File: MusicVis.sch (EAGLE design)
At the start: 14 parts, among them J1 AUDIO_JACK_3.5MM_PTH

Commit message: First pcd layout
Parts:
- added J2: 455-1750-1-ND, SparkFun-Connectors:CONN_03
- added J3: AUDIO_JACK_3.5MM_PTH, SparkFun-Connectors:AUDIO_JACK_3.5MM_PTH
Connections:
- new net 5V: B2.5V, J2.1, R6.1, VR1.E
- new net GND: B2.GND@0, B2.GND@1, B2.GND@2, C1.2, J1.SLEEVE, J2.3, J3.SLEEVE, R2.2, S1.2, S2.2, VR1.A, VR2.A
- new net N$11: B2.AREF, R3.2
- new net N$12: R1.1, R3.1, VR2.S
- new net N$14: B2.A1, VR1.S
- new net N$4: J1.TIP, J3.TIP, R5.1
- new net N$5: J1.RING, J3.RING, R4.2
- new net N$6: C2.1, R4.1, R5.2
- new net N$7: R6.2, VR2.E
- new net N$9: B2.A0, C1.1, C2.2, R1.2, R2.1
- net N$3: now also B2.D7, J2.2; no longer S1.2, S2.2
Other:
- moved on the sheet: C1, J1, R1, R2, R6, VR1

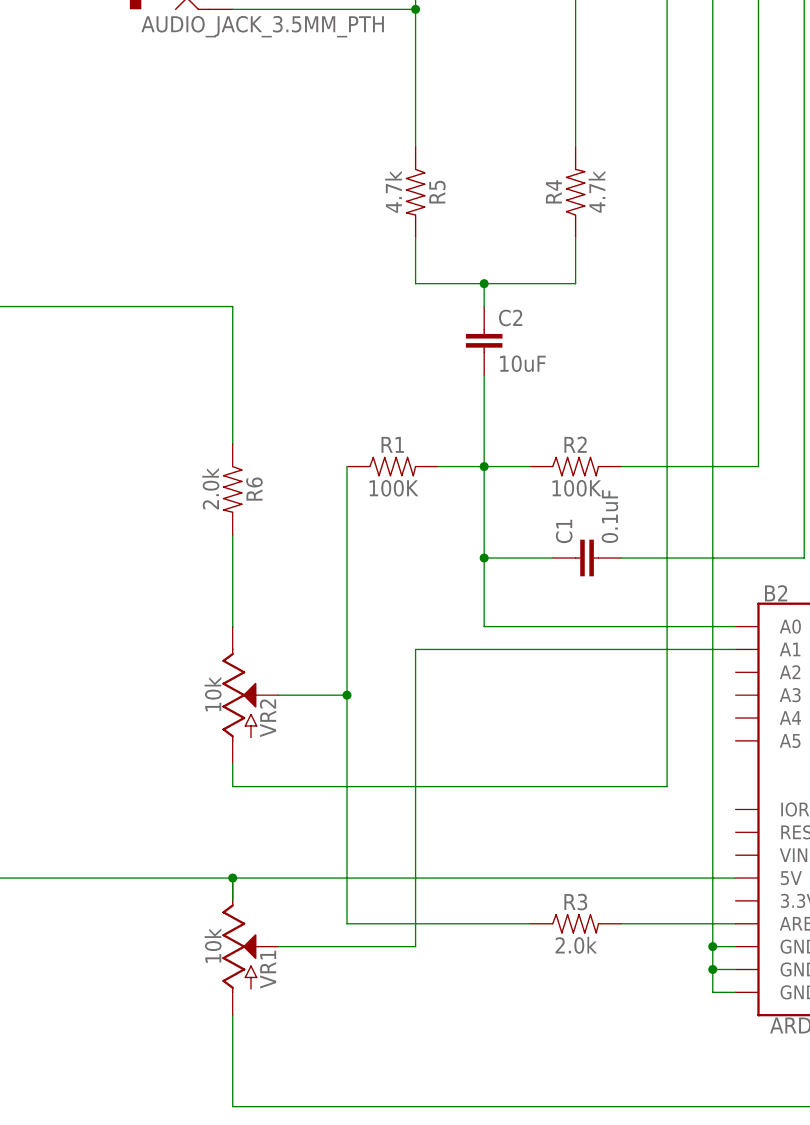
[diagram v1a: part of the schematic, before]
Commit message: Second draft of the board with pth elements and hand made connections
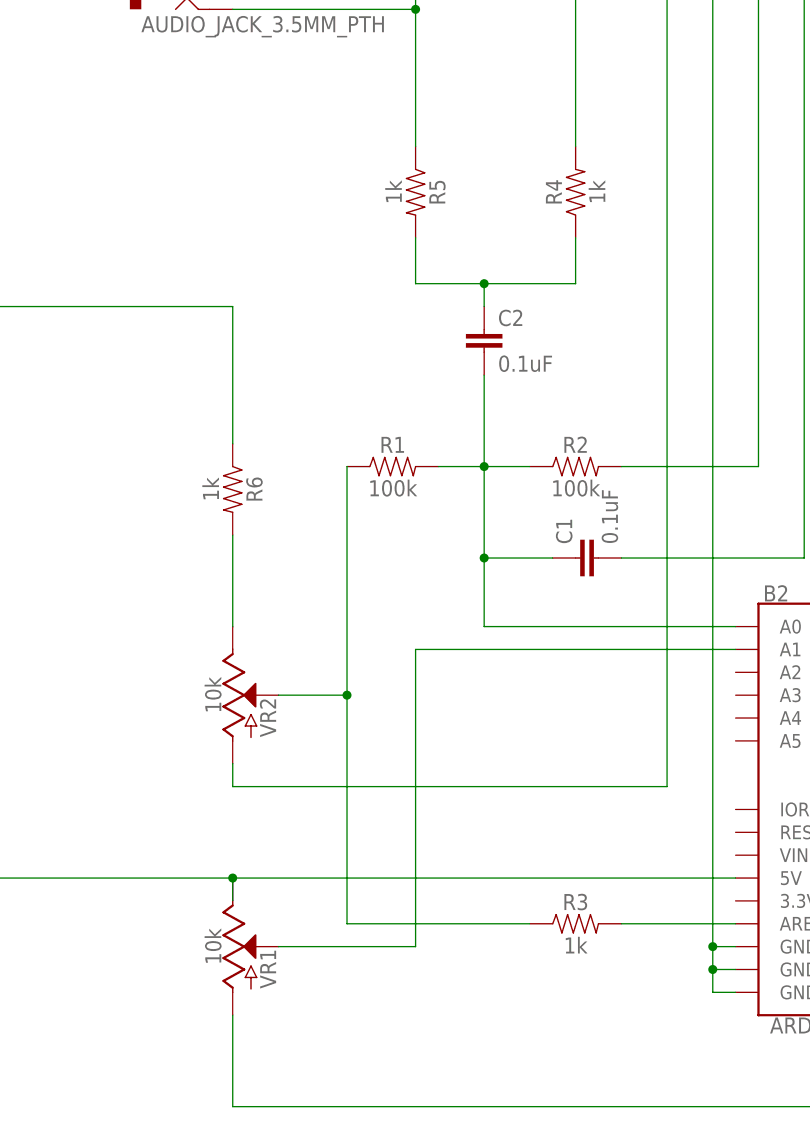
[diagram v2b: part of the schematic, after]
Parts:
- C1: device SparkFun-Capacitors:0.1UF-0402-16V-10% -> SparkFun-Capacitors:0.1UF-KIT-EZ-50V-20%
- C2: value 10uF -> 0.1uF; device SparkFun-Capacitors:10UF-0603-6.3V-20% -> SparkFun-Capacitors:0.1UF-KIT-EZ-50V-20%
- R1, R2: value 100K -> 100k; device SparkFun-Resistors:100KOHM-0402-1/16W-1% -> SparkFun-Resistors:100KOHM-HORIZ-1/4W-1%
- R3, R6: value 2.0k -> 1k; device SparkFun-Resistors:2.0KOHM-0603-1/10W-5% -> SparkFun-Resistors:1KOHM-HORIZ-1/4W-1%
- R4, R5: value 4.7k -> 1k; device SparkFun-Resistors:4.7KOHM-0603-1/10W-1% -> SparkFun-Resistors:1KOHM-HORIZ-1/4W-1%
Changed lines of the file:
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@@
 <parts>
 <part name="B2" library="SparkFun-Boards" deviceset="ARDUINO_UNO_R3_SHIELD" device="BASIC"/>
-<part name="R1" library="SparkFun-Resistors" deviceset="100KOHM" device="-0402-1/16W-1%" value="100K"/>
-<part name="R2" library="SparkFun-Resistors" deviceset="100KOHM" device="-0402-1/16W-1%" value="100K"/>
+<part name="R1" library="SparkFun-Resistors" deviceset="100KOHM" device="-HORIZ-1/4W-1%" value="100k"/>
+<part name="R2" library="SparkFun-Resistors" deviceset="100KOHM" device="-HORIZ-1/4W-1%" value="100k"/>
 <part name="SUPPLY1" library="SparkFun-PowerSymbols" deviceset="5V" device=""/>
 <part name="GND1" library="SparkFun-PowerSymbols" deviceset="GND" device=""/>
-<part name="R3" library="SparkFun-Resistors" deviceset="2.0KOHM" device="-0603-1/10W-5%" value="2.0k"/>
-<part name="R4" library="SparkFun-Resistors" deviceset="4.7KOHM" device="-0603-1/10W-1%" value="4.7k"/>
-<part name="R5" library="SparkFun-Resistors" deviceset="4.7KOHM" device="-0603-1/10W-1%" value="4.7k"/>
-<part name="R6" library="SparkFun-Resistors" deviceset="2.0KOHM" device="-0603-1/10W-5%" value="2.0k"/>
-<part name="C1" library="SparkFun-Capacitors" deviceset="0.1UF" device="-0402-16V-10%" value="0.1uF"/>
-<part name="C2" library="SparkFun-Capacitors" deviceset="10UF" device="-0603-6.3V-20%" value="10uF"/>
+<part name="R3" library="SparkFun-Resistors" deviceset="1KOHM" device="-HORIZ-1/4W-1%" value="1k"/>
+<part name="R4" library="SparkFun-Resistors" deviceset="1KOHM" device="-HORIZ-1/4W-1%" value="1k"/>
+<part name="R5" library="SparkFun-Resistors" deviceset="1KOHM" device="-HORIZ-1/4W-1%" value="1k"/>
+<part name="R6" library="SparkFun-Resistors" deviceset="1KOHM" device="-HORIZ-1/4W-1%" value="1k"/>
+<part name="C1" library="SparkFun-Capacitors" deviceset="0.1UF" device="-KIT-EZ-50V-20%" value="0.1uF"/>
+<part name="C2" library="SparkFun-Capacitors" deviceset="0.1UF" device="-KIT-EZ-50V-20%" value="0.1uF"/>
 <part name="VR1" library="SparkFun-Resistors" deviceset="POTENTIOMETER" device="-PTH-9MM-1/20W-20%" value="10k"/>
 <part name="VR2" library="SparkFun-Resistors" deviceset="POTENTIOMETER" device="-PTH-9MM-1/20W-20%" value="10k"/>
